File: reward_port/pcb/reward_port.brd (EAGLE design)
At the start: 43.2 x 64.8 mm, 28 parts

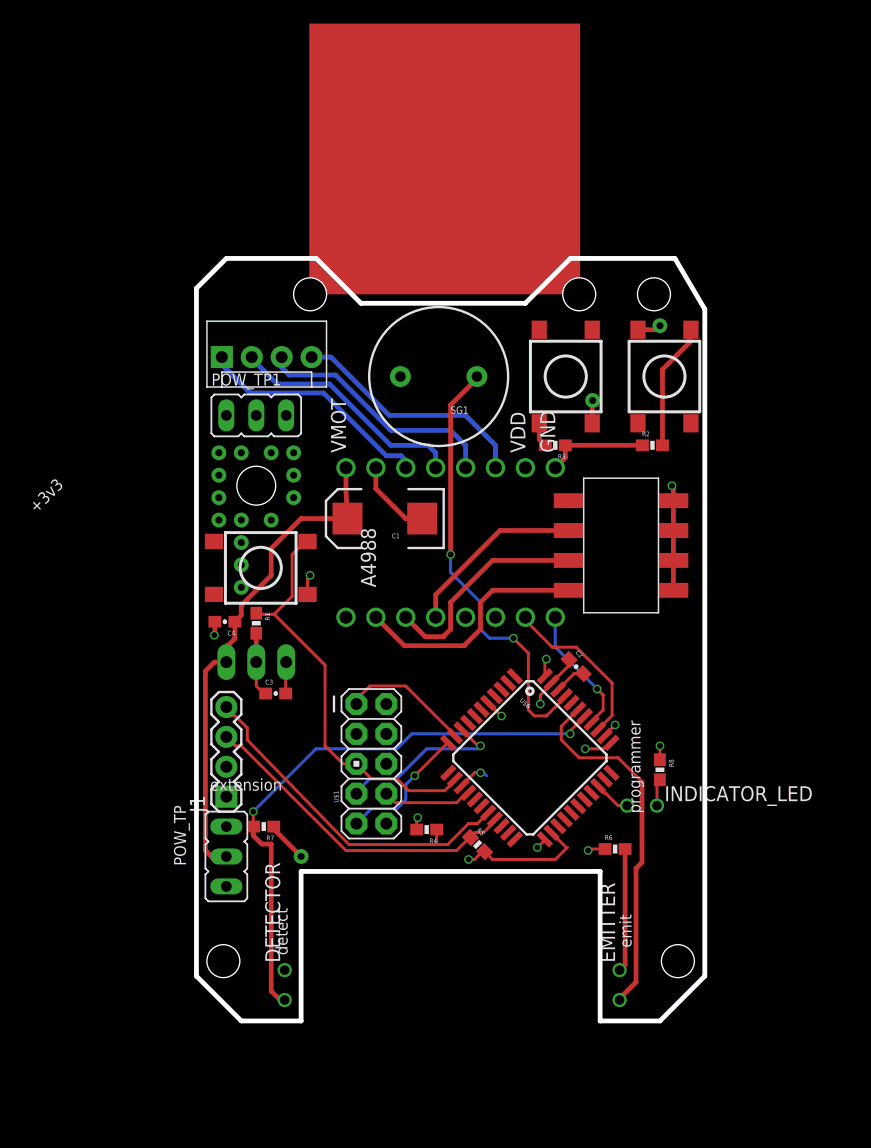
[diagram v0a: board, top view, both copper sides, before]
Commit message: test fit teensy
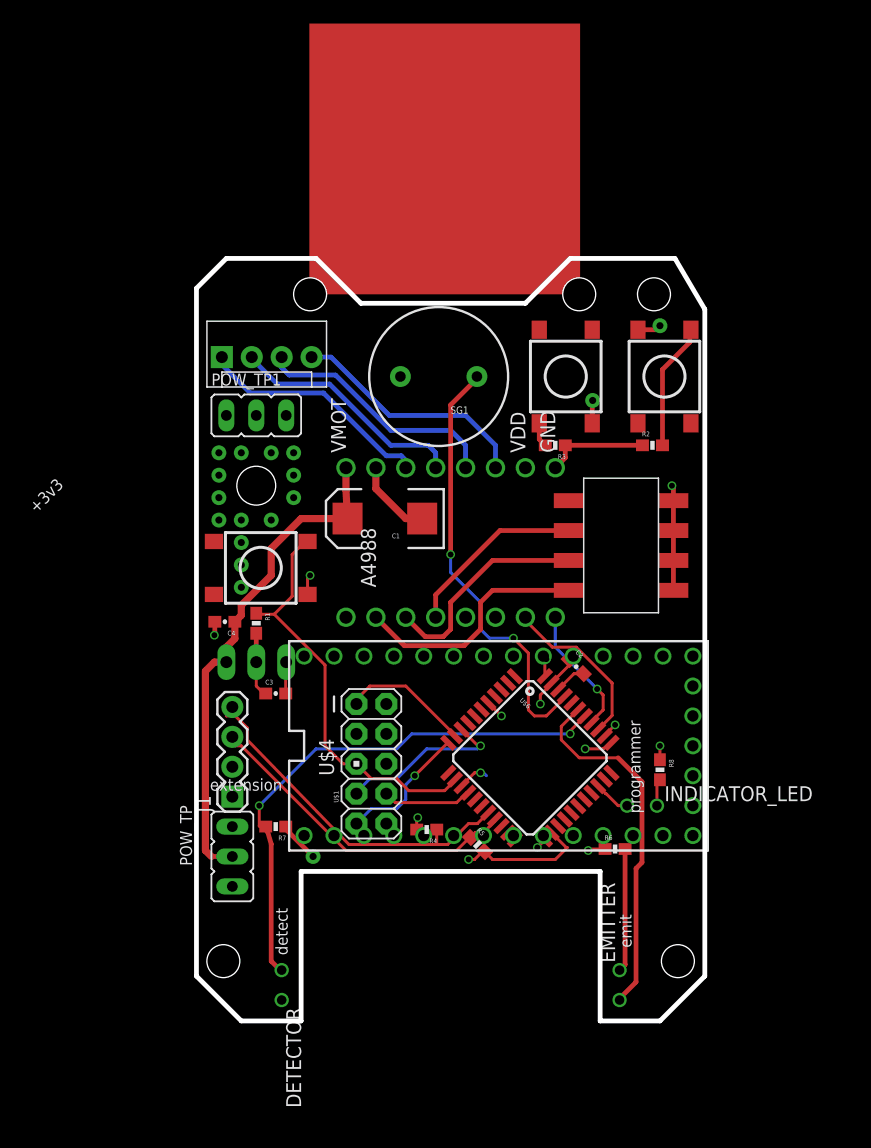
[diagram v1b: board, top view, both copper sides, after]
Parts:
- added U$4: TEENSY_3.1_OUTER_ROW, Teensy_3_and_LC_Series_Boards_v1.1:TEENSY3-OUTER_ROW
- moved R7 1.02 mm to (-14.9, 3.81)
- moved J1 0.51 mm to (-18.5, 6.35)
- moved POW_TP 0.51 mm to (-18.5, 3.81)
- moved DETECTOR 0.25 mm to (-14.4, -9.65), turned to 270 degrees
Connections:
- new net 3.3V: U$4.3.3V, U$4.3.3V1
- new net AGND: U$4.AGND
- new net VBAT: U$4.VBAT
- new net VIN: U$4.VIN
- net GND: now also U$4.GND, U$4.GND1
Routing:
- net IR_IN: track 49.5 -> 46.0 mm
- net 12V: track 42.7 -> 43.2 mm
